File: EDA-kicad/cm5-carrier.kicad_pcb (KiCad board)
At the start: 2 copper layers, 80 x 150 mm, 74 parts, among them J1 SJ2-35894B-SMT-TR, J3 SIM-G85D1160022HHR, J4 FINGER, J5 USBC-3-2-fix-USB4056-03-A_REV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, SW2 PROG, SW3 VOL-, SW4 VOL+, SW5 POW, SW6 CHP-041B, U10 BAT-CONNECTOR-FLTS22WR00, U5 Flash-LED-Lumiled, U6 FPC15pin-1mm-pitch-F52Q-1A7H1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, U7 CODEC-TLV320AIC3204IRHBR, U8 DAC-TLV320DAC3100IRHBR, U9 GSM-GPS-EC25VFA-512-STD

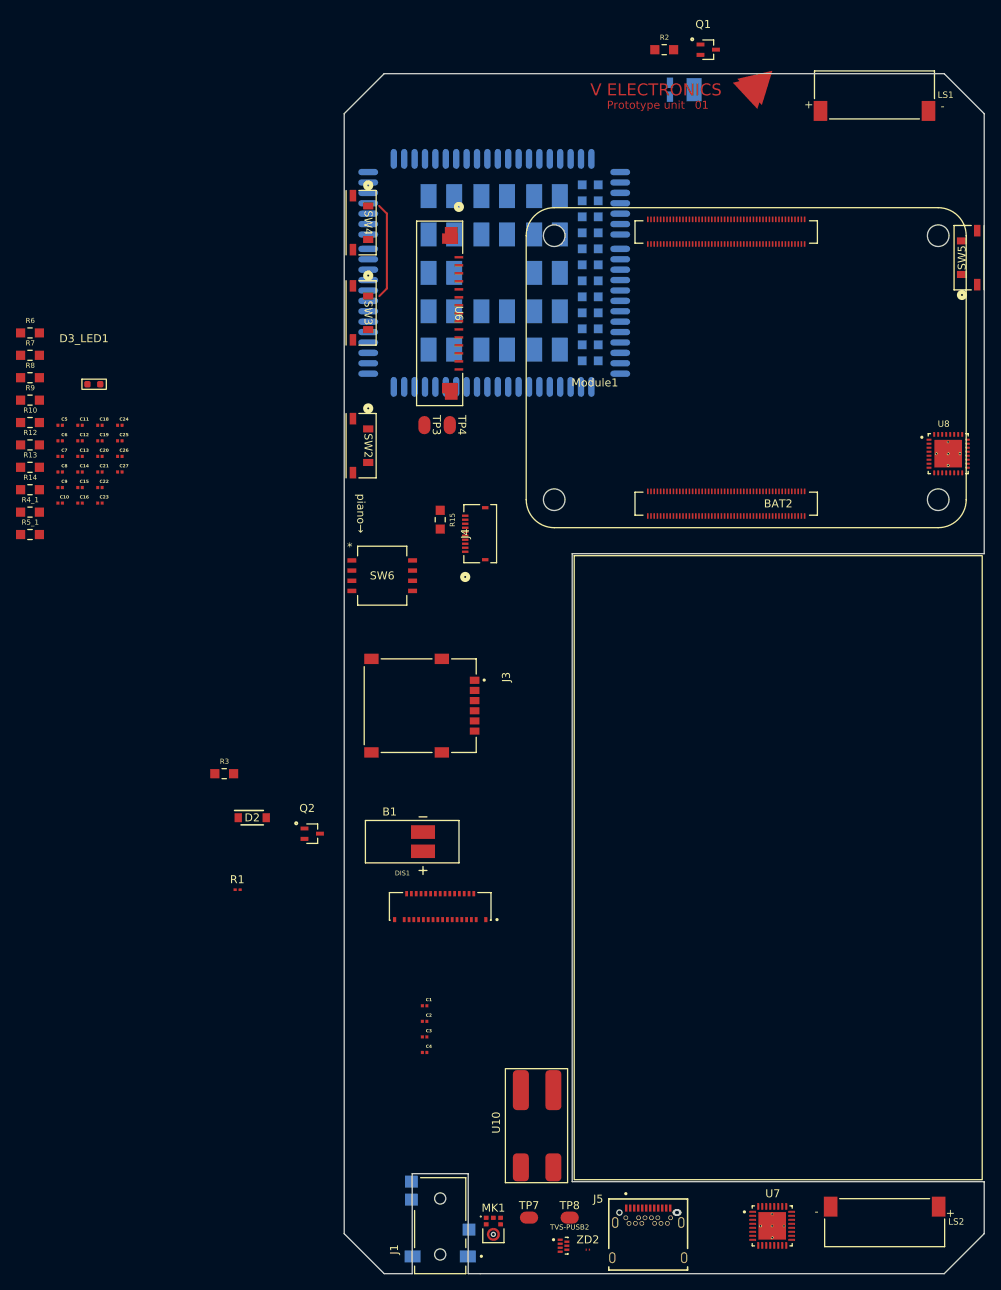
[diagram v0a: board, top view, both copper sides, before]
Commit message: fix speaker clearance issue
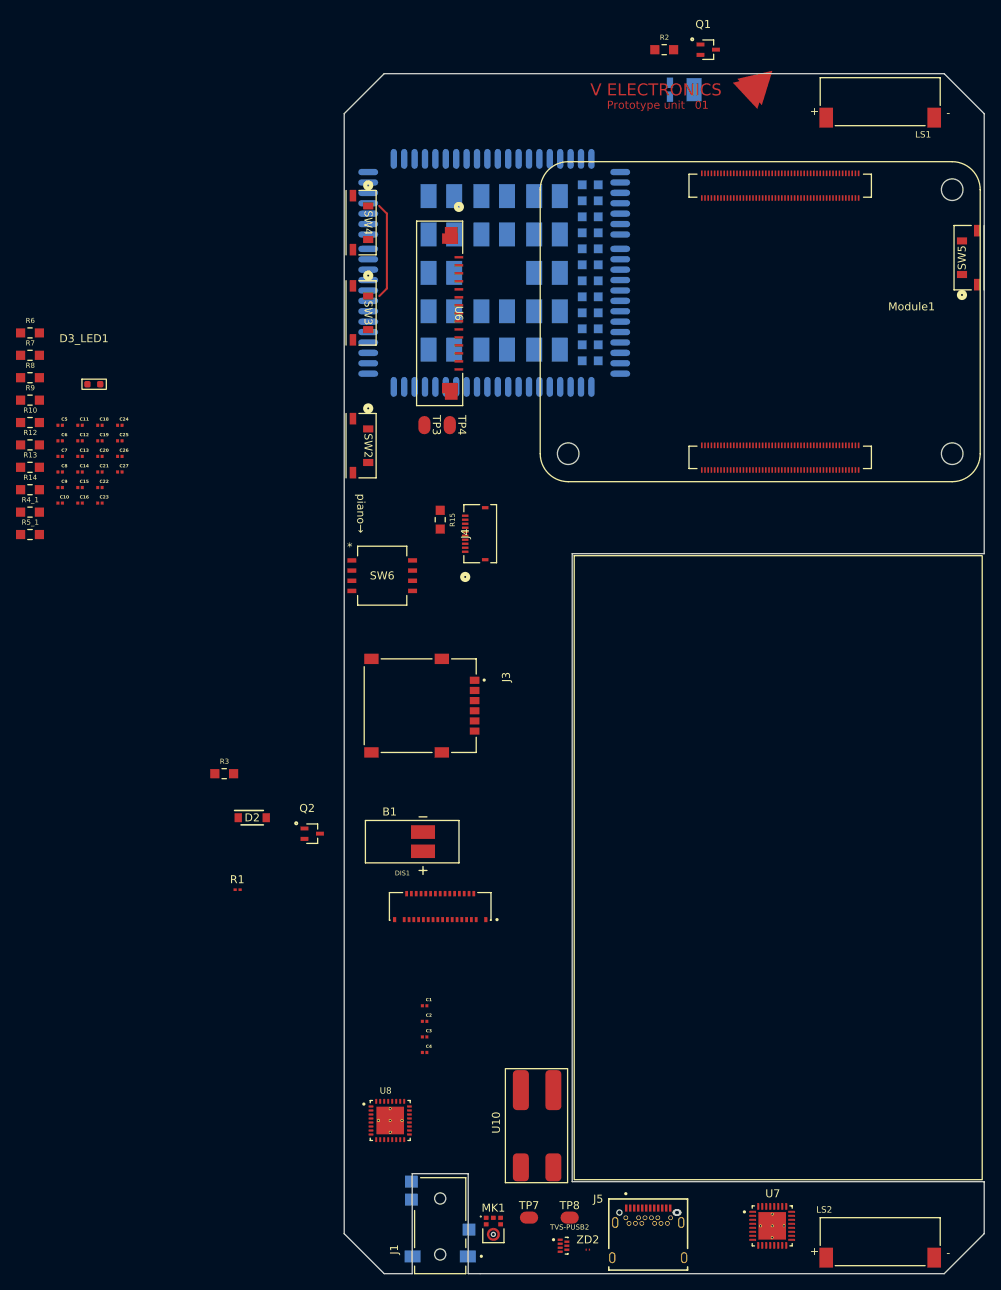
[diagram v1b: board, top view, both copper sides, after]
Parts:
- moved U8 108.7 mm to (60.8, 161.8)
- moved Module1 56.7 mm to (131.0, 78.5), turned to 90 degrees
- moved LS2 2.44 mm to (122.0, 177.0), turned to 180 degrees
- moved LS1 1.11 mm to (122.0, 34.5)
